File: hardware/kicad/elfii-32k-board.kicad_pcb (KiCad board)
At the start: 2 copper layers, 177.8 x 127.1 mm, 14 parts, among them J1 ELFII_86_MECH_UNVERIFIED, SW1 RAM_PAGE_ENABLE, U1 74HC573, U2 CY62256-70PC, U3 74HC151, U4 CD4011

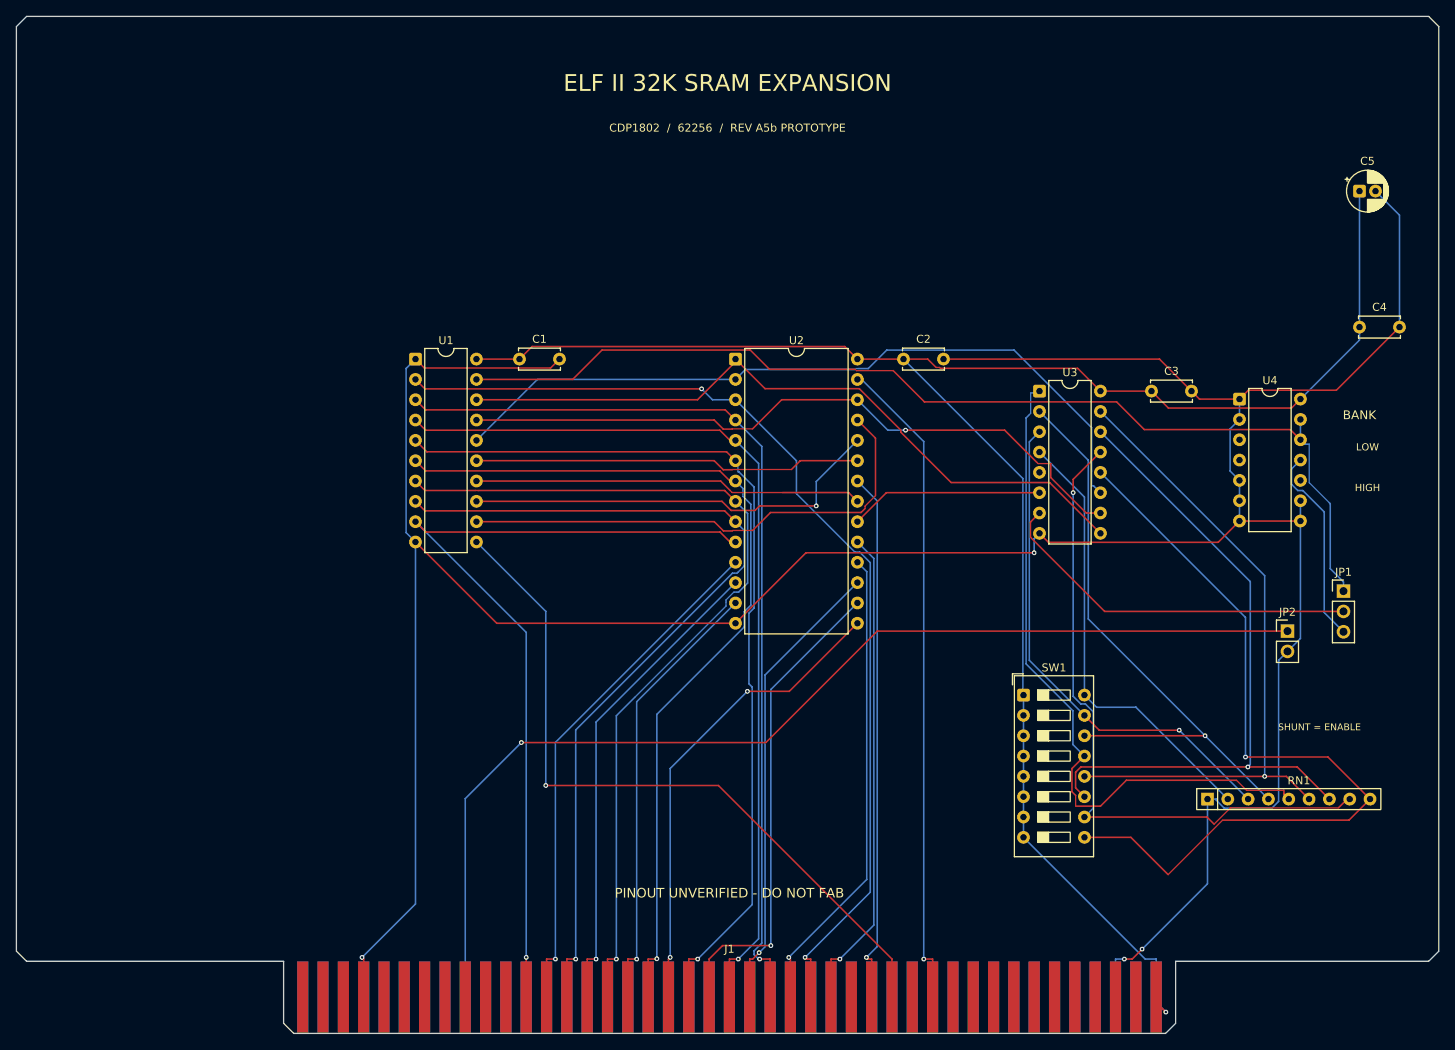
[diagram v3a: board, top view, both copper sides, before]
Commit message: Move +5V layer tie above edge-finger bevel; add two setback GND pours for review
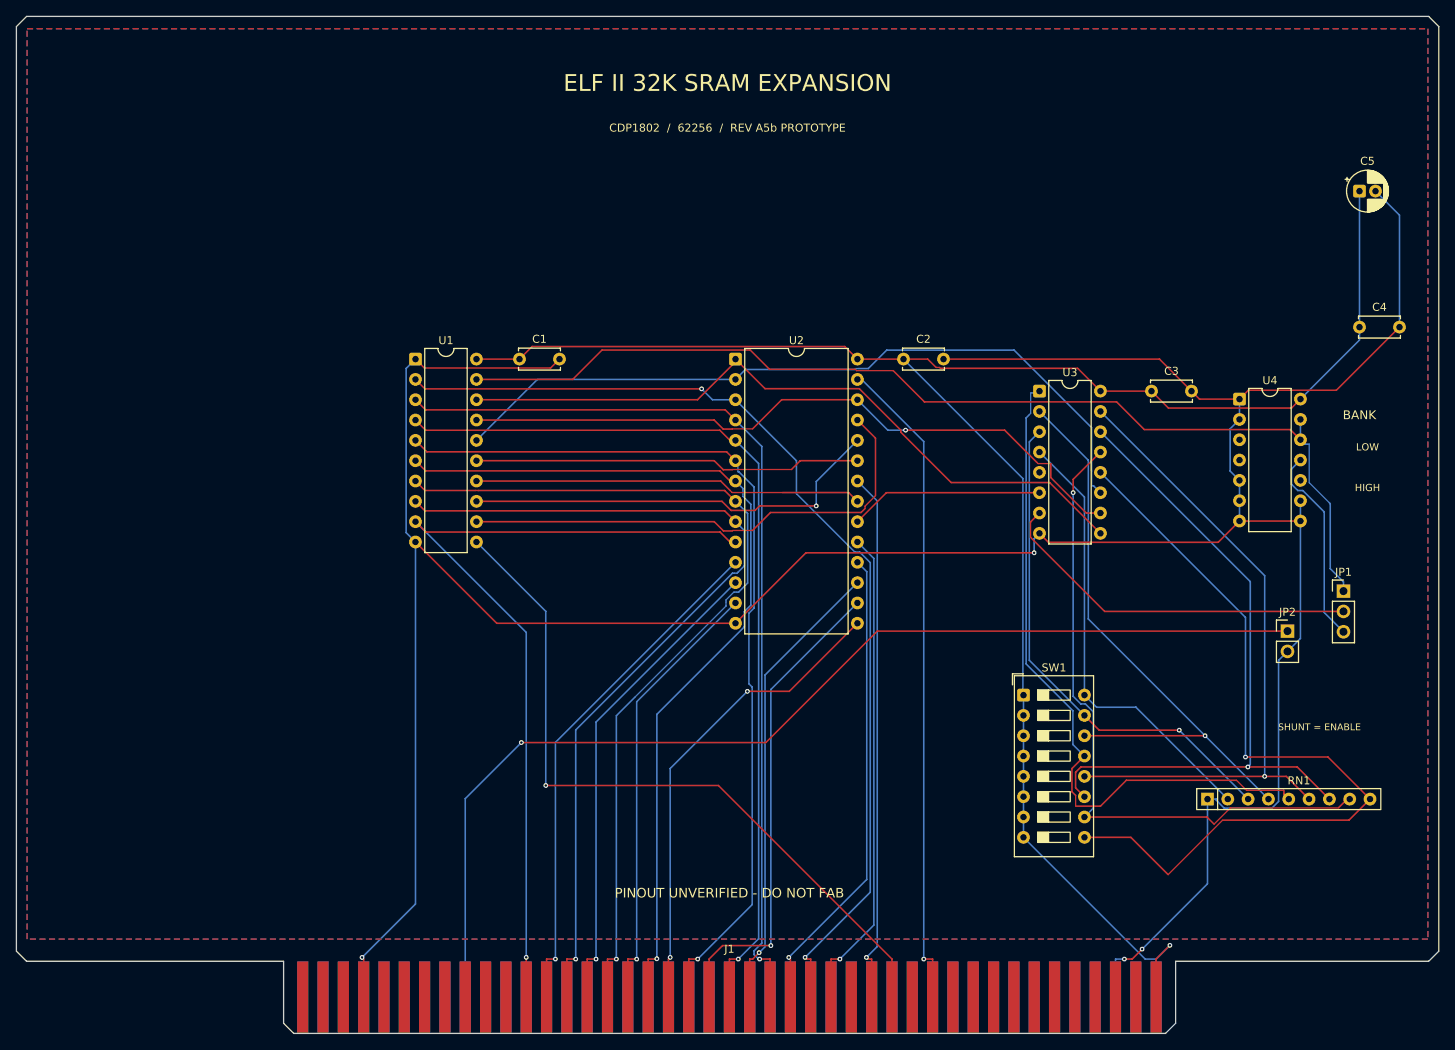
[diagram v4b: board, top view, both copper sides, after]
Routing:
- net +5V: track 234.7 -> 239.6 mm
- added copper zone on B.Cu, net GND
- added copper zone on F.Cu, net GND
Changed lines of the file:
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@@
-	)
-	(segment
-		(start 174.793 150.627)
-		(end 173.5836 149.4176)
-		(width 0.2)
-		(layer "F.Cu")
-		(net 26)
 	)
 	(segment
@@
 	)
 	(segment
-		(start 173.5836 149.4176)
-		(end 173.5836 148.7424)
-		(width 0.2)
-		(layer "F.Cu")
-		(net 26)
-	)
-	(segment
 		(start 146.0696 70.0396)
 		(end 145.03 69)
@@
 		(net 26)
 	)
-	(via
-		(at 174.793 150.627)
-		(size 0.6)
-		(drill 0.3)
-		(layers "F.Cu" "B.Cu")
-		(net 26)
-	)
-	(segment
-		(start 174.793 150.627)
-		(end 173.5836 149.4176)
-		(width 0.2)
-		(layer "B.Cu")
-		(net 26)
-	)
 	(segment
 		(start 157 128.78)
@@
 		(start 191.62 74)
 		(end 199 66.62)
-		(width 0.2)
-		(layer "B.Cu")
-		(net 26)
-	)
-	(segment
-		(start 173.5836 149.4176)
-		(end 173.5836 148.7424)
 		(width 0.2)
 		(layer "B.Cu")
@@
 	)
 	(embedded_fonts no)
+	(segment
+		(start 173.5836 148.7424)
+		(end 173.5836 143.9957)
+		(width 0.2)
+		(layer "F.Cu")
+		(net 26)
+	)
+	(segment
+		(start 173.5836 143.9957)
+		(end 175.3 142.2793)
+		(width 0.2)
+		(layer "F.Cu")
+		(net 26)
+	)
+	(segment
+		(start 173.5836 143.9957)
+		(end 175.3 142.2793)
+		(width 0.2)
+		(layer "B.Cu")
+		(net 26)
+	)
+	(via
+		(at 175.3 142.2793)
+		(size 0.6)
+		(drill 0.3)
+		(layers "F.Cu" "B.Cu")
+		(net 26)
+	)
+	(zone
+		(net 27)
+		(net_name "GND")
+		(layer "F.Cu")
+		(hatch edge 0.508)
+		(connect_pads
+			(clearance 0.3)
+		)
+		(min_thickness 0.2)
+		(fill yes
+			(thermal_gap 0.3)
+			(thermal_bridge_width 0.3)
+			(island_removal_mode 1)
+			(island_area_min 10)
+		)
+		(polygon
+			(pts
+				(xy 32.45 27.7) (xy 207.55 27.7)
+				(xy 207.55 141.5) (xy 32.45 141.5)
+			)
+		)
+	)
+	(zone
+		(net 27)
+		(net_name "GND")
+		(layer "B.Cu")
+		(hatch edge 0.508)
+		(connect_pads
+			(clearance 0.3)
+		)
+		(min_thickness 0.2)
+		(fill yes
+			(thermal_gap 0.3)
+			(thermal_bridge_width 0.3)
+			(island_removal_mode 1)
+			(island_area_min 10)
+		)
+		(polygon
+			(pts
+				(xy 32.45 27.7) (xy 207.55 27.7)
+				(xy 207.55 141.5) (xy 32.45 141.5)
+			)
+		)
+	)
 )
